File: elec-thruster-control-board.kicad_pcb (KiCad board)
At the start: 2 copper layers, 55.5 x 67 mm, 55 parts, among them J1 gp8-pwm4A, J13 Conn_01x07, J22 Conn_01x06, J24 Conn_01x06, J3 gp8-pwm4A, J4 Conn_01x20_Socket, J6 Conn_01x20_Socket

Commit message: Ok heres the final final final final version mkay
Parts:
- added C1: C, Capacitor_SMD:C_0805_2012Metric, F.Cu at (151.2, 110.2)
- added C2: C, Capacitor_SMD:C_0805_2012Metric, F.Cu at (121.5, 113.8)
- added R19: R, Resistor_SMD:R_0805_2012Metric, F.Cu at (148.5, 108.8)
- added R20: R, Resistor_SMD:R_0805_2012Metric, F.Cu at (129.5, 108.8)
- moved R11 12.1 mm to (125.8, 113.0), turned to 90 degrees
- moved R18 9.18 mm to (151.2, 105.0), turned to -90 degrees
- moved R12 8.00 mm to (150.5, 113.5), turned to 0 degrees
- moved D11 4.42 mm to (147.0, 112.8)
- moved R17 3.66 mm to (127.0, 108.8), turned to -90 degrees
- moved D12 3.46 mm to (129.5, 112.8)
- moved D14 3.15 mm to (143.6, 112.8)
- moved R14 3.15 mm to (143.5, 108.8)
- moved D15 1.65 mm to (140.1, 112.8)
- moved R15 1.65 mm to (140.0, 108.8)
- moved D13 1.35 mm to (133.0, 112.8)
- moved R13 1.35 mm to (133.0, 108.8)
- moved J1 0.37 mm to (122.2, 107.8)
- moved D16 0.15 mm to (136.6, 112.8)
- moved R16 0.15 mm to (136.5, 108.8)
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- renumbered TH9 to J11, TH1 to J12, TH3 to J15, TH4 to J16, TH8 to J18, TH7 to J19, TH0 to J2, TH6 to J20, TH5 to J21, TH2 to J5
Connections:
- J13 pad 6: Net-(J1-Pin_2) -> Net-(J13-Pin_6)
- J3 pad 2: Net-(J13-Pin_1) -> Net-(J3-Pin_2)
- J4 pad 20: Net-(J1-Pin_2) -> Net-(J13-Pin_6)
- R11 pad 1: GND -> Net-(D12-A)
- R12 pad 2: Net-(J13-Pin_1) -> Net-(J3-Pin_2)
- R17 pad 1: Net-(D12-A) -> GND
- R18 pad 2: Net-(J13-Pin_1) -> Net-(J3-Pin_2)
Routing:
- net Net-(J3-Pin_2): track 0.00 -> 21.8 mm
- net Net-(J13-Pin_6): track 0.00 -> 15.4 mm
- net Net-(J13-Pin_1): track 44.5 -> 33.1 mm
- net Net-(J1-Pin_2): track 25.0 -> 17.2 mm
- net Net-(D12-A): track 2.11 -> 5.56 mm
- net Net-(D11-A): track 2.16 -> 4.21 mm
- net Net-(J13-Pin_3): track 24.4 -> 25.8 mm
- net Net-(J13-Pin_5): track 19.1 -> 18.3 mm
- net Net-(J13-Pin_4): track 22.3 -> 23.1 mm
- net GND: track 0.87 -> 0.67 mm, vias 18 -> 20
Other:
- board text added: "D13"

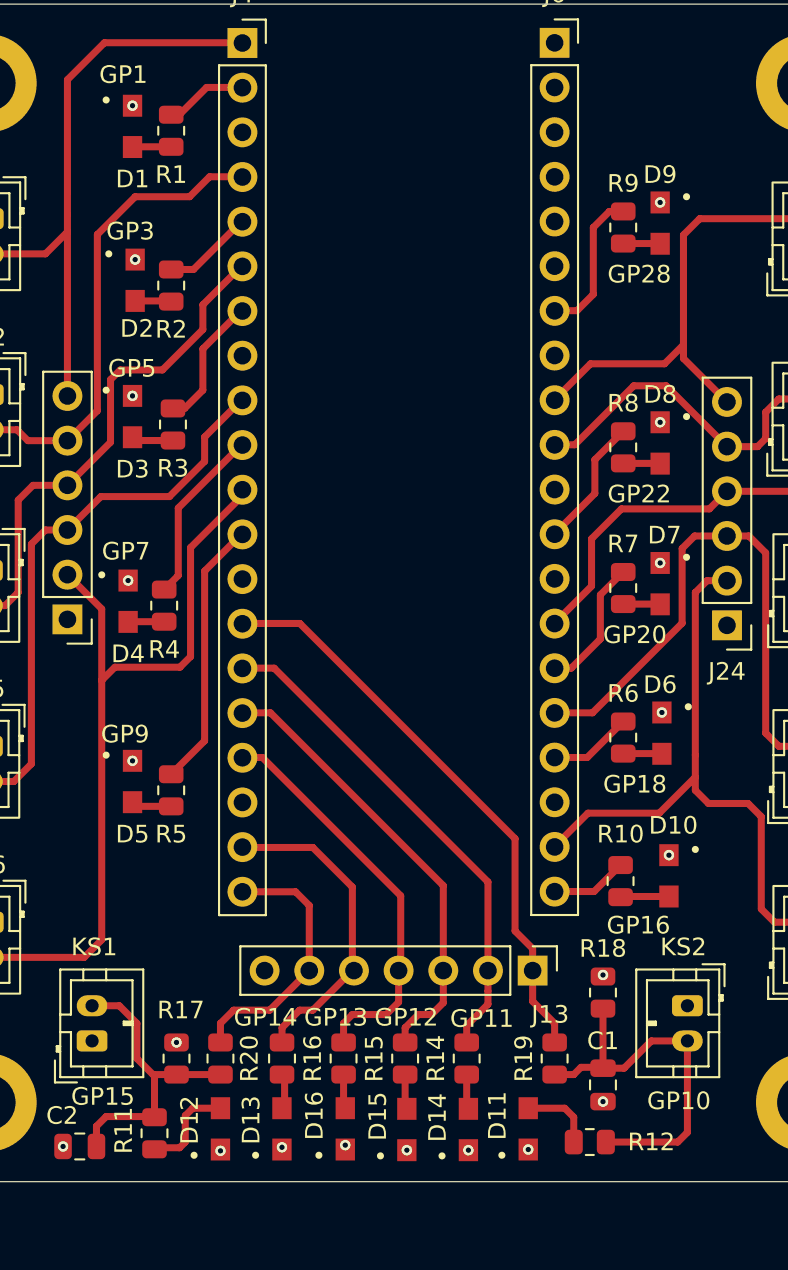
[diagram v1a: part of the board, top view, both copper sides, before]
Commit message: Completed BOM (and updated connector and resistors values to be correct)
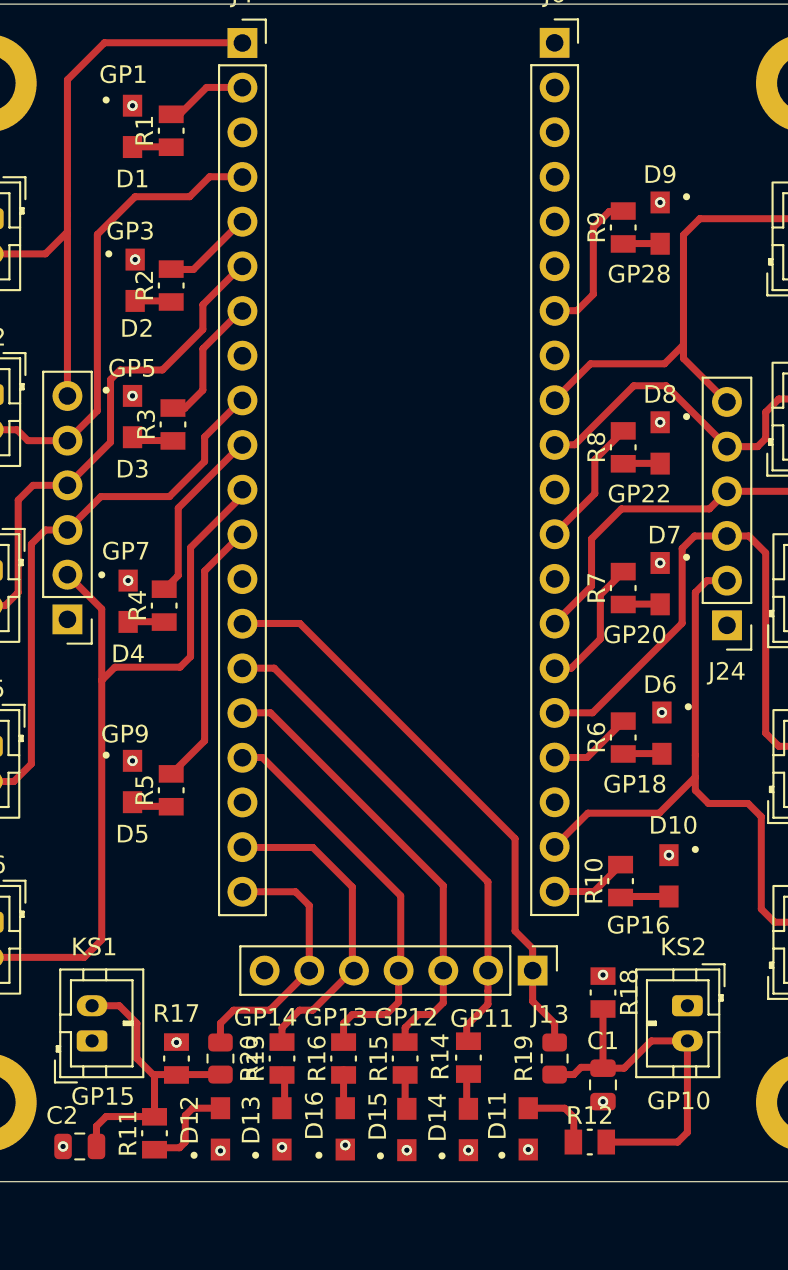
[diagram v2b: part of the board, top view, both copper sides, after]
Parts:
- C1, C2: value C -> 1uF
- R1, R10, R11, R12, R13, R14, R15, R16, R17, R18, R2, R3, R4, R5, R6, R7, R8, R9: value R -> 330; footprint Resistor_SMD:R_0805_2012Metric -> RNCF0805DTE330R:RESC2012X65N
- R19, R20: value R -> 1k
- moved R14 0.11 mm to (143.6, 108.7)

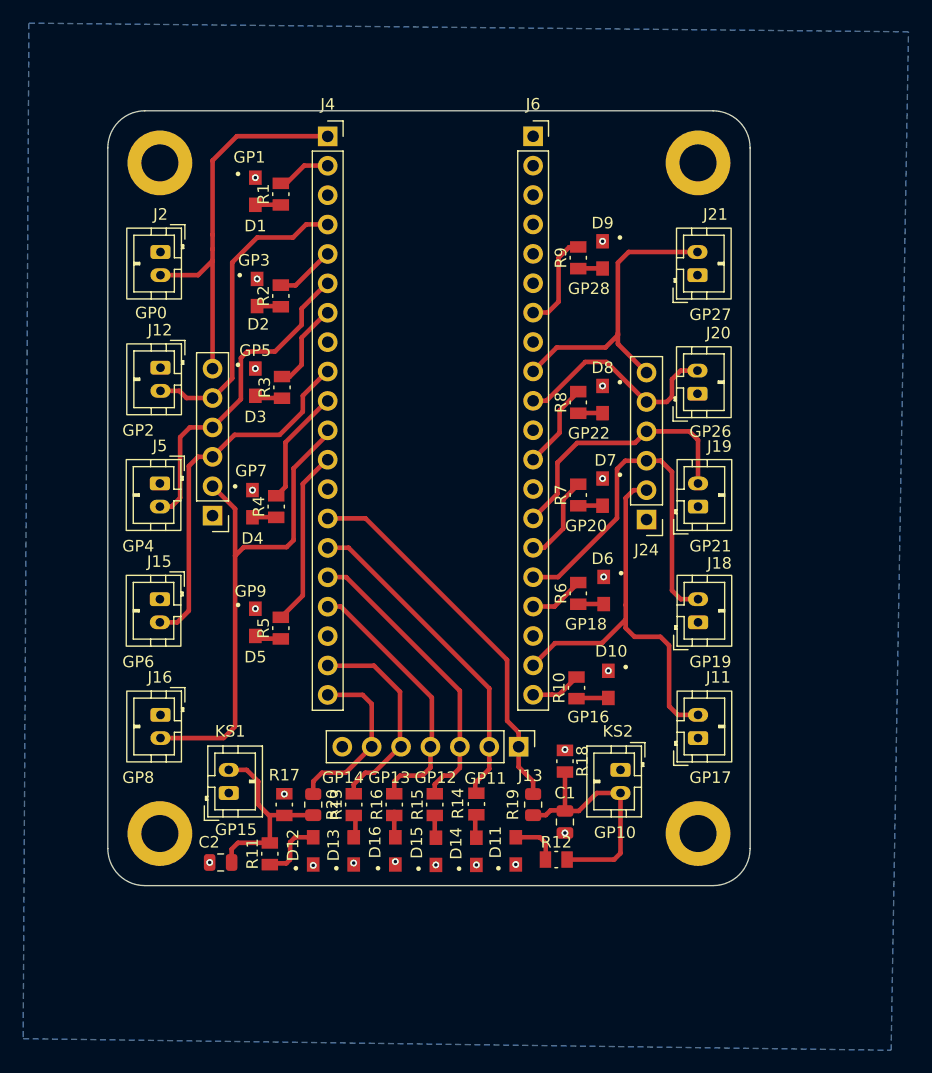
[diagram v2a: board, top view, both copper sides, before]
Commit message: Final Draft of the Board (Hopefully Finalized) Updated all footprints to match parts in BOM Moved reference designators to proper locations (as importing new footprints moved them) Moved Kill switch connectors to have silkscreen labels more visible (no longer symmetrical, but there should be adequate spacing between parts
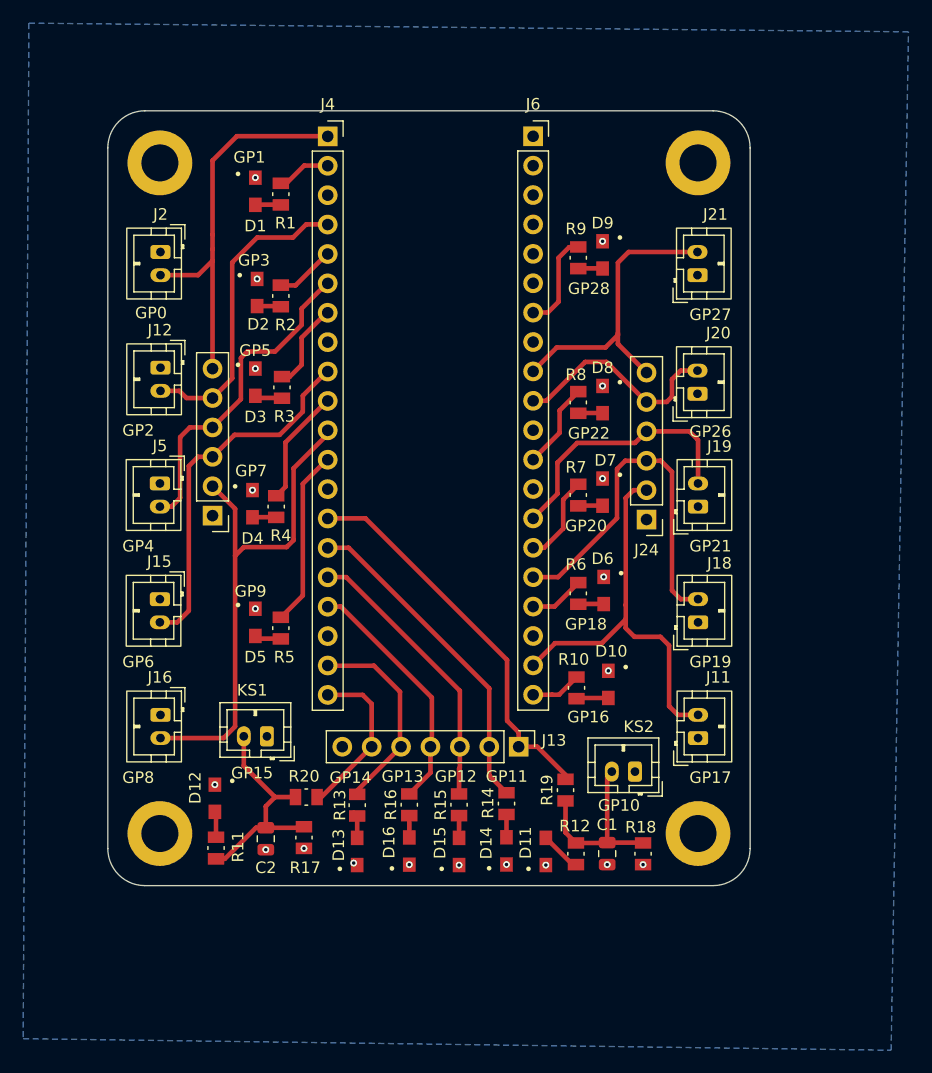
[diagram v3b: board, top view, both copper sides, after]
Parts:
- J1: value gp8-pwm4A -> gp15-pwm7B
- J3: value gp8-pwm4A -> gp10-pwm5A
- R19, R20: value 1k -> 4.7k; footprint Resistor_SMD:R_0805_2012Metric -> Imported Footprints:RESC2012X65N
- moved R18 10.5 mm to (158.0, 113.0), turned to 90 degrees
- moved D12 9.64 mm to (121.0, 108.2), turned to -90 degrees
- moved J1 5.91 mm to (125.5, 102.8), turned to 180 degrees
- moved R11 4.68 mm to (121.1, 112.5), turned to -90 degrees
- moved C1 4.56 mm to (154.9, 113.0)
- moved C2 4.41 mm to (125.4, 111.7), turned to -90 degrees
- moved R17 3.32 mm to (128.7, 111.6), turned to 90 degrees
- moved R19 3.07 mm to (151.3, 107.5)
- moved D11 2.60 mm to (149.6, 112.8)
- moved D14 2.60 mm to (146.2, 112.8)
- moved R14 2.60 mm to (146.2, 108.7)
- moved R15 2.10 mm to (142.1, 108.8)
- moved D15 2.00 mm to (142.1, 112.8)
- moved R12 1.77 mm to (152.2, 113.0), turned to 90 degrees
- moved R16 1.30 mm to (137.8, 108.8)
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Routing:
- net Net-(J3-Pin_2): track 21.8 -> 16.2 mm
- net Net-(D12-A): track 5.56 -> 2.23 mm
- net Net-(J1-Pin_2): track 17.2 -> 19.9 mm
- net Net-(J13-Pin_4): track 23.1 -> 21.4 mm
- net Net-(J13-Pin_3): track 25.8 -> 24.5 mm
- net Net-(J13-Pin_6): track 15.4 -> 14.5 mm
- net Net-(J13-Pin_1): track 33.1 -> 34.0 mm
- net Net-(D11-A): track 4.21 -> 3.56 mm

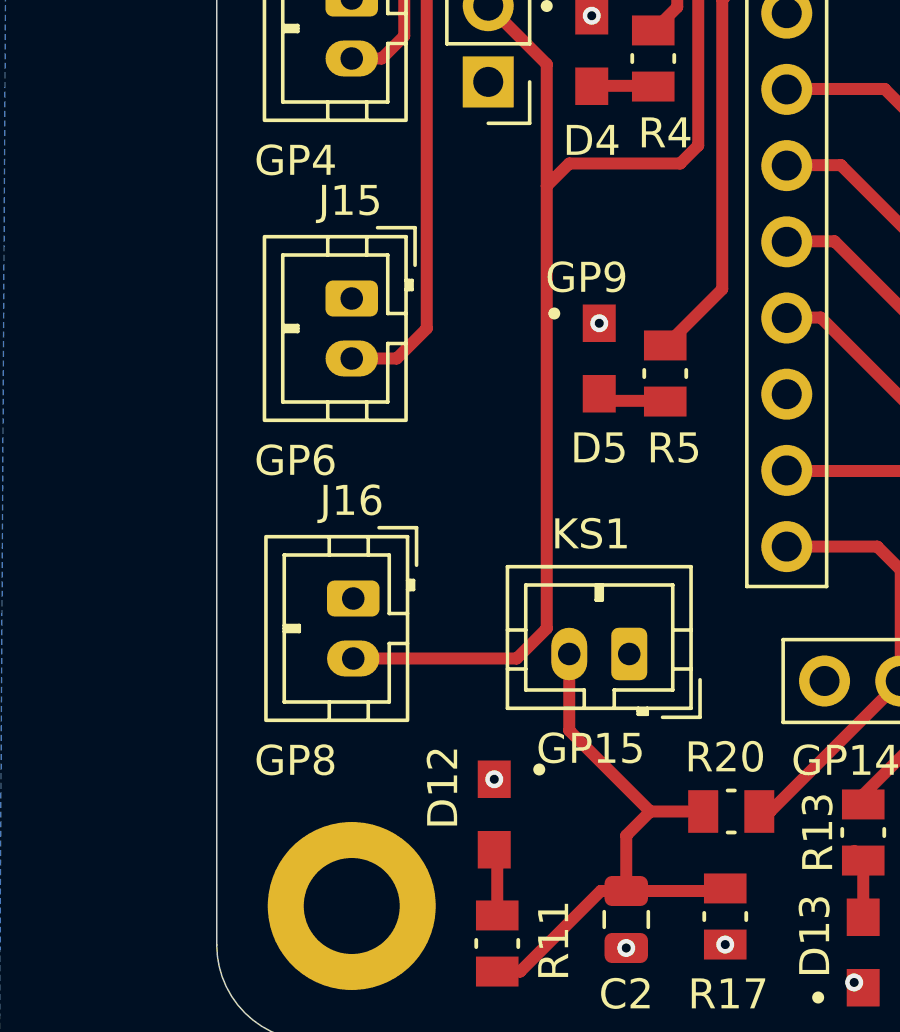
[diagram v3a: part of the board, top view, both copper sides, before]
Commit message: Ran DRC and fixed errors
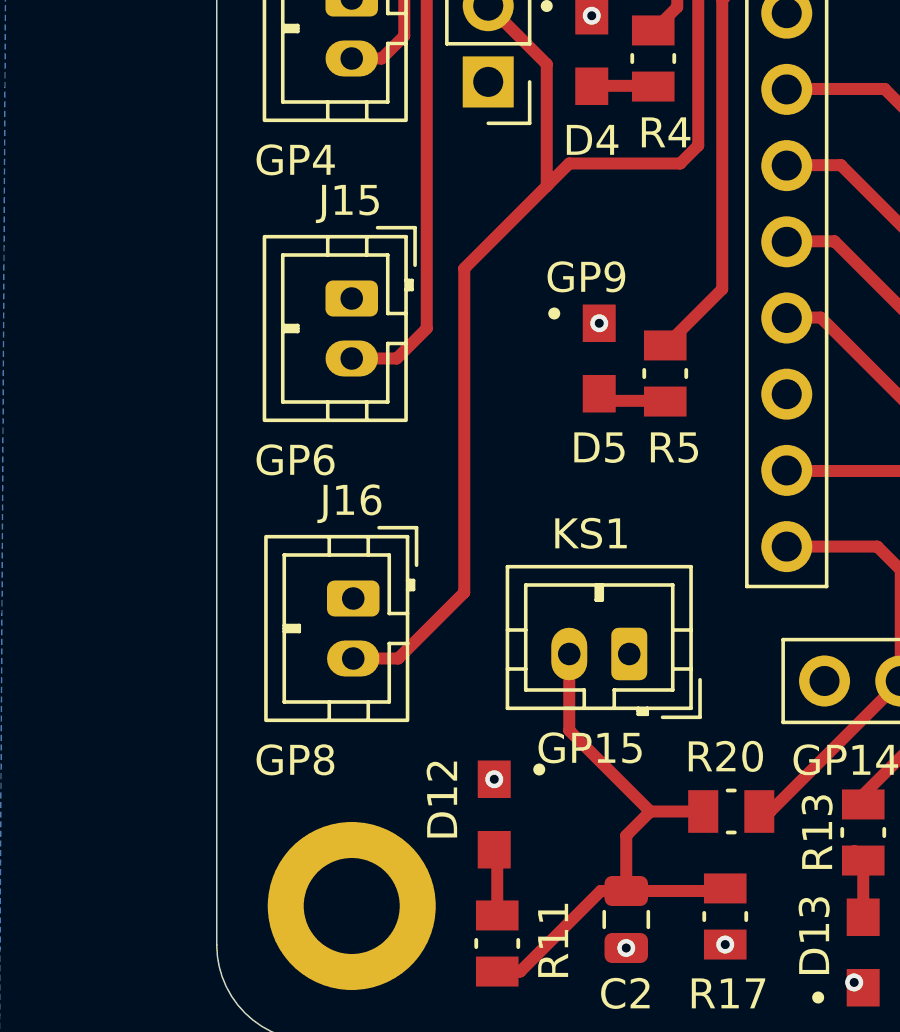
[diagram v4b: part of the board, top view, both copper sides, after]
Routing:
- net /gp8-pwm4A: track 44.7 -> 42.4 mm
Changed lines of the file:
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@@
 		(at 121 108.2 -90)
 		(property "Reference" "D12"
-			(at -0.9 1.7 90)
+			(at -0.5 1.7 90)
 			(layer "F.SilkS")
 			(effects
@@
 	)
 	(segment
-		(start 122.75 102)
-		(end 121.75 103)
+		(start 116.3 103)
+		(end 117.8 103)
 		(width 0.4)
 		(layer "F.Cu")
@@
 	)
 	(segment
+		(start 117.8 103)
+		(end 120 100.8)
+		(width 0.4)
+		(layer "F.Cu")
+		(net 3)
+	)
+	(segment
 		(start 130.6975 76.395)
 		(end 130.6975 76.8025)
@@
 	)
 	(segment
-		(start 121.75 103)
-		(end 116.3 103)
+		(start 122.75 87.25)
+		(end 120 90)
 		(width 0.4)
 		(layer "F.Cu")
@@
 	)
 	(segment
-		(start 122.75 87.25)
-		(end 122.75 102)
+		(start 120 100.8)
+		(end 120 90)
 		(width 0.4)
 		(layer "F.Cu")
@@
 	)
 	(segment
-		(start 154.9 112.035)
-		(end 154.9 106.3)
-		(width 0.4)
-		(layer "F.Cu")
-		(net 49)
-	)
-	(segment
 		(start 154.87 112.065)
 		(end 154.9 112.035)
@@
 		(width 0.4)
 		(layer "F.Cu")
+		(net 49)
+	)
+	(segment
+		(start 154.9 112.035)
+		(end 154.9 106.3)
+		(width 0.4)
+		(layer "F.Cu")
